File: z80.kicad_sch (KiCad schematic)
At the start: 34 parts, among them IC4 Z80CPU, IC5 64k_SRAM_Z80, U3 TL972

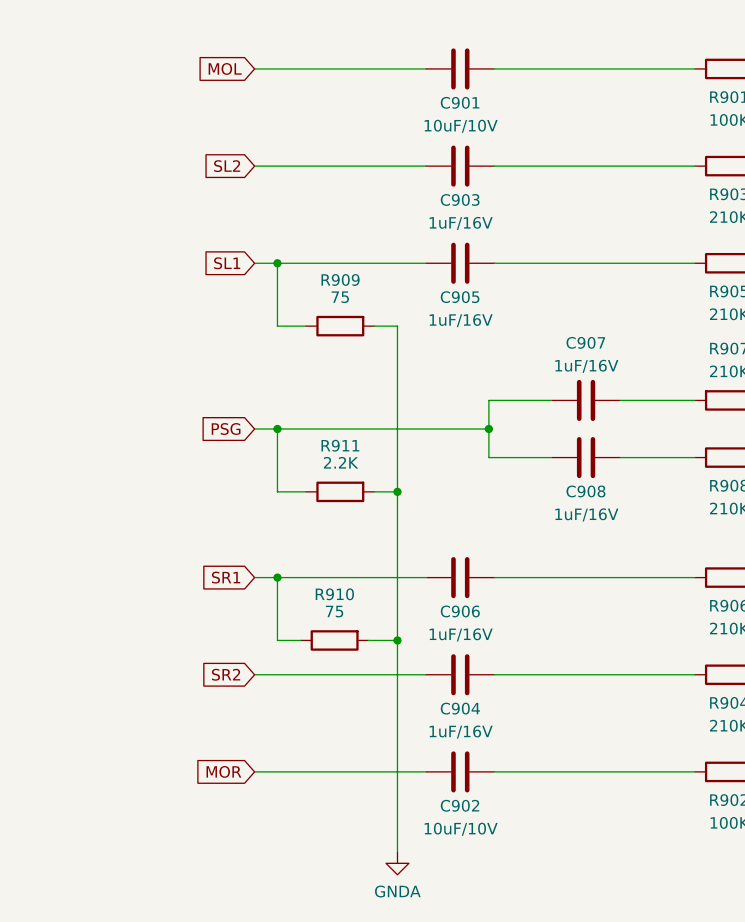
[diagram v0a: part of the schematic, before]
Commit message: Pulldowns for SL2/SR2.
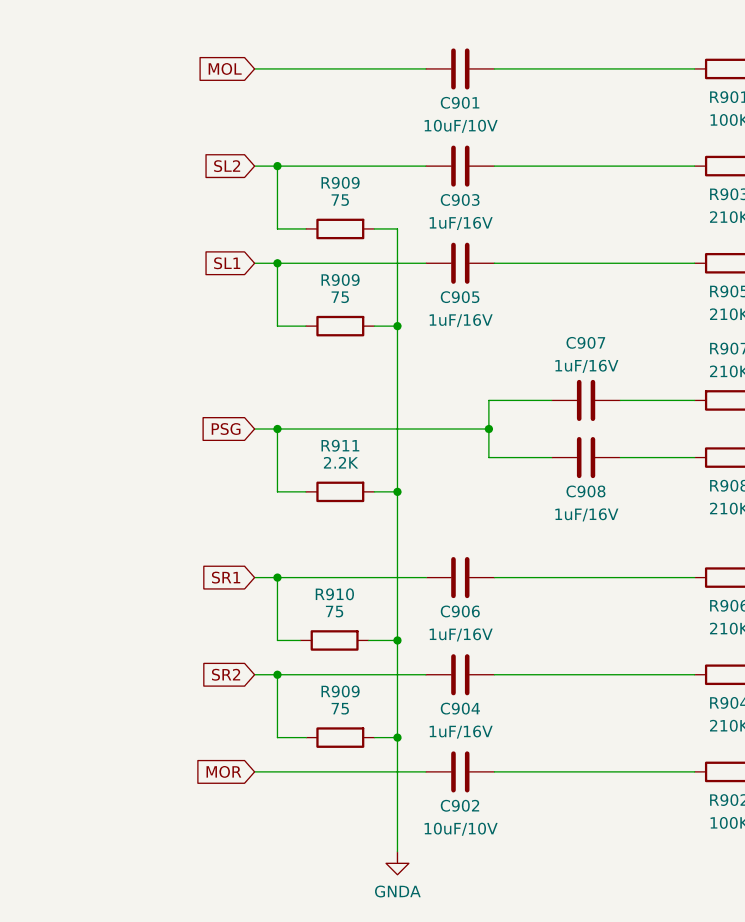
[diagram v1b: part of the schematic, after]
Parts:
- added R909 (x2): 75, symbol Device:R
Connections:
- net GNDA: now also R909.2, R909.2
- net SL2: now also R909.1
- net SR2: now also R909.1
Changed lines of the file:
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@@
   (junction (at 116.84 236.22) (diameter 0) (color 0 0 0 0)
   )
+  (junction (at 72.39 248.92) (diameter 0) (color 0 0 0 0)
+  )
   (junction (at 116.84 241.935) (diameter 0) (color 0 0 0 0)
   )
@@
   (junction (at 191.77 129.54) (diameter 0) (color 0 0 0 0)
   )
+  (junction (at 59.055 185.42) (diameter 0) (color 0 0 0 0)
+  )
   (junction (at 110.49 129.54) (diameter 0) (color 0 0 0 0)
   )
+  (junction (at 72.39 203.2) (diameter 0) (color 0 0 0 0)
+  )
   (junction (at 141.605 214.63) (diameter 0) (color 0 0 0 0)
   )
@@
   )
   (junction (at 59.055 196.215) (diameter 0) (color 0 0 0 0)
+  )
+  (junction (at 59.055 241.935) (diameter 0) (color 0 0 0 0)
   )
   (junction (at 126.365 227.33) (diameter 0) (color 0 0 0 0)
@@
     (stroke (width 0) (type default))
   )
+  (wire (pts (xy 72.39 248.92) (xy 72.39 261.62))
+    (stroke (width 0) (type default))
+  )
   (wire (pts (xy 125.73 60.325) (xy 140.97 60.325))
     (stroke (width 0) (type default))
@@
     (stroke (width 0) (type default))
   )
+  (wire (pts (xy 59.055 248.92) (xy 59.055 241.935))
+    (stroke (width 0) (type default))
+  )
   (bus (pts (xy 123.19 34.29) (xy 123.19 50.165))
     (stroke (width 0) (type default))
@@
     (stroke (width 0) (type default))
   )
+  (wire (pts (xy 72.39 192.405) (xy 72.39 203.2))
+    (stroke (width 0) (type default))
+  )
   (bus (pts (xy 191.77 73.025) (xy 191.77 129.54))
     (stroke (width 0) (type default))
@@
     (stroke (width 0) (type default))
   )
+  (wire (pts (xy 59.055 241.935) (xy 75.565 241.935))
+    (stroke (width 0) (type default))
+  )
   (wire (pts (xy 214.63 114.3) (xy 214.63 127))
     (stroke (width 0) (type default))
@@
     (stroke (width 0) (type default))
   )
-  (wire (pts (xy 56.515 241.935) (xy 75.565 241.935))
+  (wire (pts (xy 56.515 241.935) (xy 59.055 241.935))
     (stroke (width 0) (type default))
   )
@@
     (stroke (width 0) (type default))
   )
-  (wire (pts (xy 56.515 185.42) (xy 75.565 185.42))
+  (wire (pts (xy 56.515 185.42) (xy 59.055 185.42))
     (stroke (width 0) (type default))
   )
@@
     (stroke (width 0) (type default))
   )
+  (wire (pts (xy 69.85 192.405) (xy 72.39 192.405))
+    (stroke (width 0) (type default))
+  )
   (wire (pts (xy 165.735 233.68) (xy 161.29 233.68))
     (stroke (width 0) (type default))
@@
     (stroke (width 0) (type default))
   )
-  (wire (pts (xy 72.39 238.125) (xy 72.39 261.62))
+  (wire (pts (xy 72.39 238.125) (xy 72.39 248.92))
     (stroke (width 0) (type default))
   )
@@
     (stroke (width 0) (type default))
   )
+  (wire (pts (xy 69.85 248.92) (xy 72.39 248.92))
+    (stroke (width 0) (type default))
+  )
   (wire (pts (xy 176.53 67.945) (xy 189.23 67.945))
     (stroke (width 0) (type default))
@@
     (stroke (width 0) (type default))
   )
+  (wire (pts (xy 59.055 192.405) (xy 59.055 185.42))
+    (stroke (width 0) (type default))
+  )
   (wire (pts (xy 92.71 111.125) (xy 107.95 111.125))
     (stroke (width 0) (type default))
@@
     (stroke (width 0) (type default))
   )
+  (wire (pts (xy 59.055 185.42) (xy 75.565 185.42))
+    (stroke (width 0) (type default))
+  )
   (wire (pts (xy 165.735 185.42) (xy 165.735 174.625))
     (stroke (width 0) (type default))
@@
     (stroke (width 0) (type default))
   )
+  (wire (pts (xy 62.23 192.405) (xy 59.055 192.405))
+    (stroke (width 0) (type default))
+  )
   (wire (pts (xy 92.71 78.105) (xy 107.95 78.105))
     (stroke (width 0) (type default))
@@
   )
   (wire (pts (xy 57.15 102.235) (xy 43.18 102.235))
+    (stroke (width 0) (type default))
+  )
+  (wire (pts (xy 62.23 248.92) (xy 59.055 248.92))
     (stroke (width 0) (type default))
   )
@@
         (path "/bcc23b51-b742-4ae5-9dd6-d96a24058944/293c8f1f-2c58-4557-aeb8-8502bb66fbd4"
           (reference "#PWR010") (unit 1)
+        )
+      )
+    )
+  )
+  (symbol (lib_id "Device:R") (at 66.04 192.405 90) (mirror x) (unit 1)
+    (in_bom yes) (on_board yes) (dnp no)
+    (property "Reference" "R909" (at 66.04 187.325 90)
+      (effects (font (size 1.27 1.27)))
+    )
+    (property "Value" "75" (at 66.04 189.23 90)
+      (effects (font (size 1.27 1.27)))
+    )
+    (property "Footprint" "" (at 66.04 190.627 90)
+      (effects (font (size 1.27 1.27)) hide)
+    )
+    (property "Datasheet" "~" (at 66.04 192.405 0)
+      (effects (font (size 1.27 1.27)) hide)
+    )
+    (pin "1")
+    (pin "2")
+    (instances
+      (project "Neptune"
+        (path "/bcc23b51-b742-4ae5-9dd6-d96a24058944/01513199-62c5-4123-a151-ccd381a5e6c1"
+          (reference "R909") (unit 1)
+        )
+        (path "/bcc23b51-b742-4ae5-9dd6-d96a24058944/293c8f1f-2c58-4557-aeb8-8502bb66fbd4"
+          (reference "R911") (unit 1)
         )
       )
@@
         )
         (path "/bcc23b51-b742-4ae5-9dd6-d96a24058944/293c8f1f-2c58-4557-aeb8-8502bb66fbd4"
-          (reference "R910") (unit 1)
+          (reference "R916") (unit 1)
         )
       )
@@
         )
         (path "/bcc23b51-b742-4ae5-9dd6-d96a24058944/293c8f1f-2c58-4557-aeb8-8502bb66fbd4"
-          (reference "R911") (unit 1)
+          (reference "R913") (unit 1)
         )
       )
@@
         )
         (path "/bcc23b51-b742-4ae5-9dd6-d96a24058944/293c8f1f-2c58-4557-aeb8-8502bb66fbd4"
-          (reference "R913") (unit 1)
+          (reference "R919") (unit 1)
         )
       )
@@
         )
         (path "/bcc23b51-b742-4ae5-9dd6-d96a24058944/293c8f1f-2c58-4557-aeb8-8502bb66fbd4"
-          (reference "R911") (unit 1)
+          (reference "R917") (unit 1)
         )
       )
@@
         )
         (path "/bcc23b51-b742-4ae5-9dd6-d96a24058944/293c8f1f-2c58-4557-aeb8-8502bb66fbd4"
-          (reference "R912") (unit 1)
+          (reference "R918") (unit 1)
         )
       )
@@
         )
       )
+    )
+  )
+  (symbol (lib_id "Device:R") (at 66.04 248.92 90) (mirror x) (unit 1)
+    (in_bom yes) (on_board yes) (dnp no)
+    (property "Reference" "R909" (at 66.04 243.84 90)
+      (effects (font (size 1.27 1.27)))
+    )
+    (property "Value" "75" (at 66.04 245.745 90)
+      (effects (font (size 1.27 1.27)))
+    )
+    (property "Footprint" "" (at 66.04 247.142 90)
+      (effects (font (size 1.27 1.27)) hide)
+    )
+    (property "Datasheet" "~" (at 66.04 248.92 0)
+      (effects (font (size 1.27 1.27)) hide)
+    )
+    (pin "1")
+    (pin "2")
+    (instances
+      (project "Neptune"
+        (path "/bcc23b51-b742-4ae5-9dd6-d96a24058944/01513199-62c5-4123-a151-ccd381a5e6c1"
+          (reference "R909") (unit 1)
+        )
+        (path "/bcc23b51-b742-4ae5-9dd6-d96a24058944/293c8f1f-2c58-4557-aeb8-8502bb66fbd4"
+          (reference "R912") (unit 1)
+        )
+      )

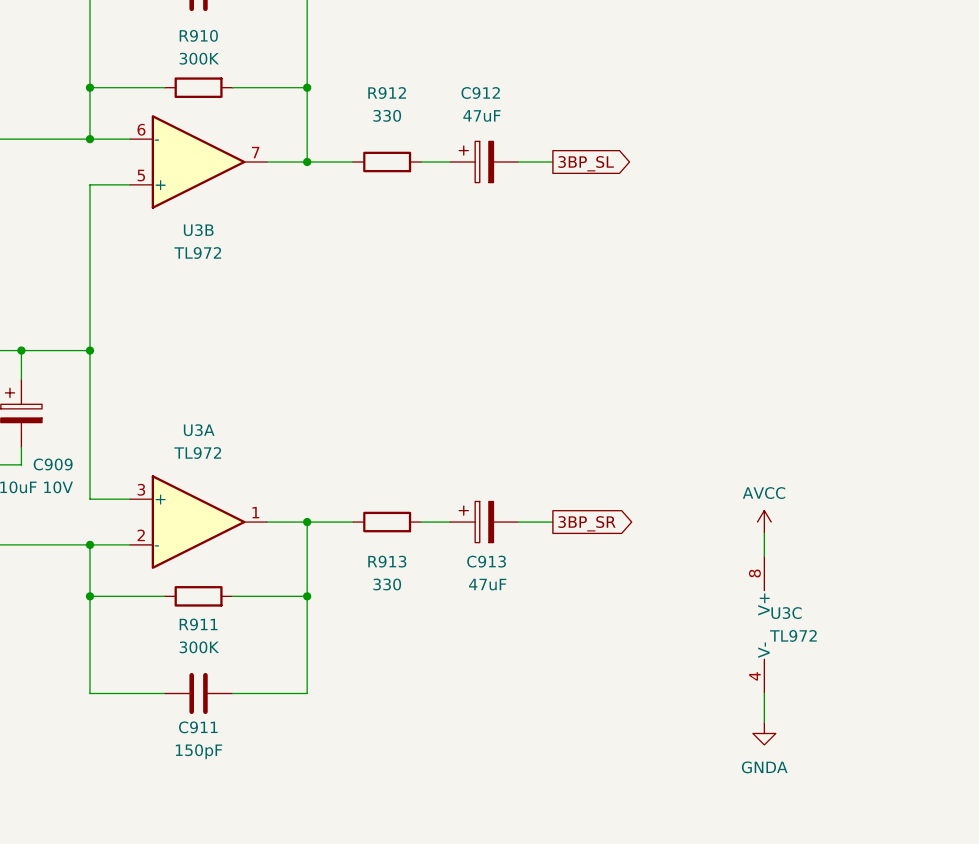
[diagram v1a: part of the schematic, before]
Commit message: Shared op-amp for audio and reset.
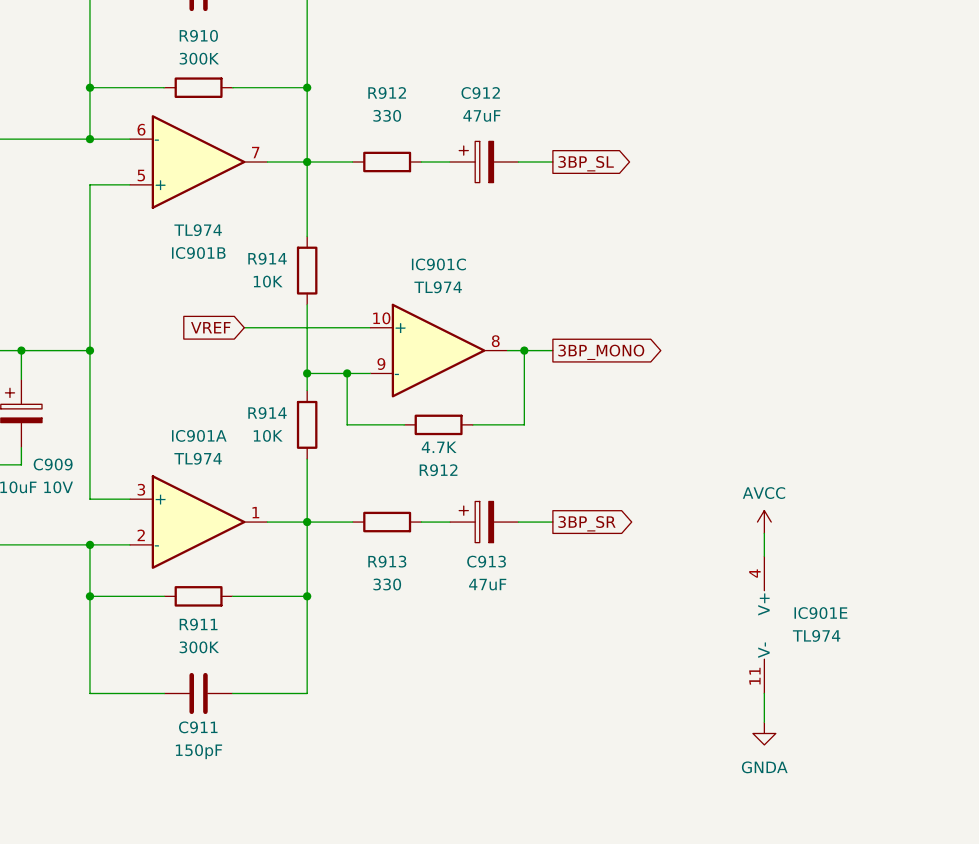
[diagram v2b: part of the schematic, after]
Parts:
- removed U3: TL972, symbol Amplifier_Operational:TL062
- added IC901: TL974, symbol Amplifier_Operational:TL064
- added R912: 4.7K, symbol Device:R
- added R914 (x2): 10K, symbol Device:R
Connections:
- net AVCC: now also IC901.4 (V+)
- net GNDA: now also IC901.11 (V-)
- net at C910.1, R901.2, R903.2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: now also IC901.6 (-)
- net at C910.2, R910.2, R912.1: now also IC901.7, R914.2
- net at C911.1, R902.2, R904.2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: now also IC901.2 (-)
- net at C909.1, R914.1, R915.2: now also IC901.3 (+), IC901.5 (+)
- net at C911.2, R911.2, R913.1: now also IC901.1, R914.1
- new net: IC901.9 (-), R912.1, R914.1, R914.2
- new net 3BP_MONO: IC901.8, R912.2
- new net VREF: IC901.10 (+)
